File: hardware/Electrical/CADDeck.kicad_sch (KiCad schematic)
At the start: 26 parts, among them SW1L SW_Push, SW1R SW_Push, SW2L SW_Push, SW2R SW_Push, SW3L SW_Push, SW3R SW_Push, SW4L SW_Push, SW4R SW_Push, SW5L SW_Push, SW5R SW_Push, U4 49E Zoom, U5 39E Rotate, U6 TTP223

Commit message: Alles aktualisiert
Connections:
- net at U1. (VDD): now also R6.2, SW3L.2

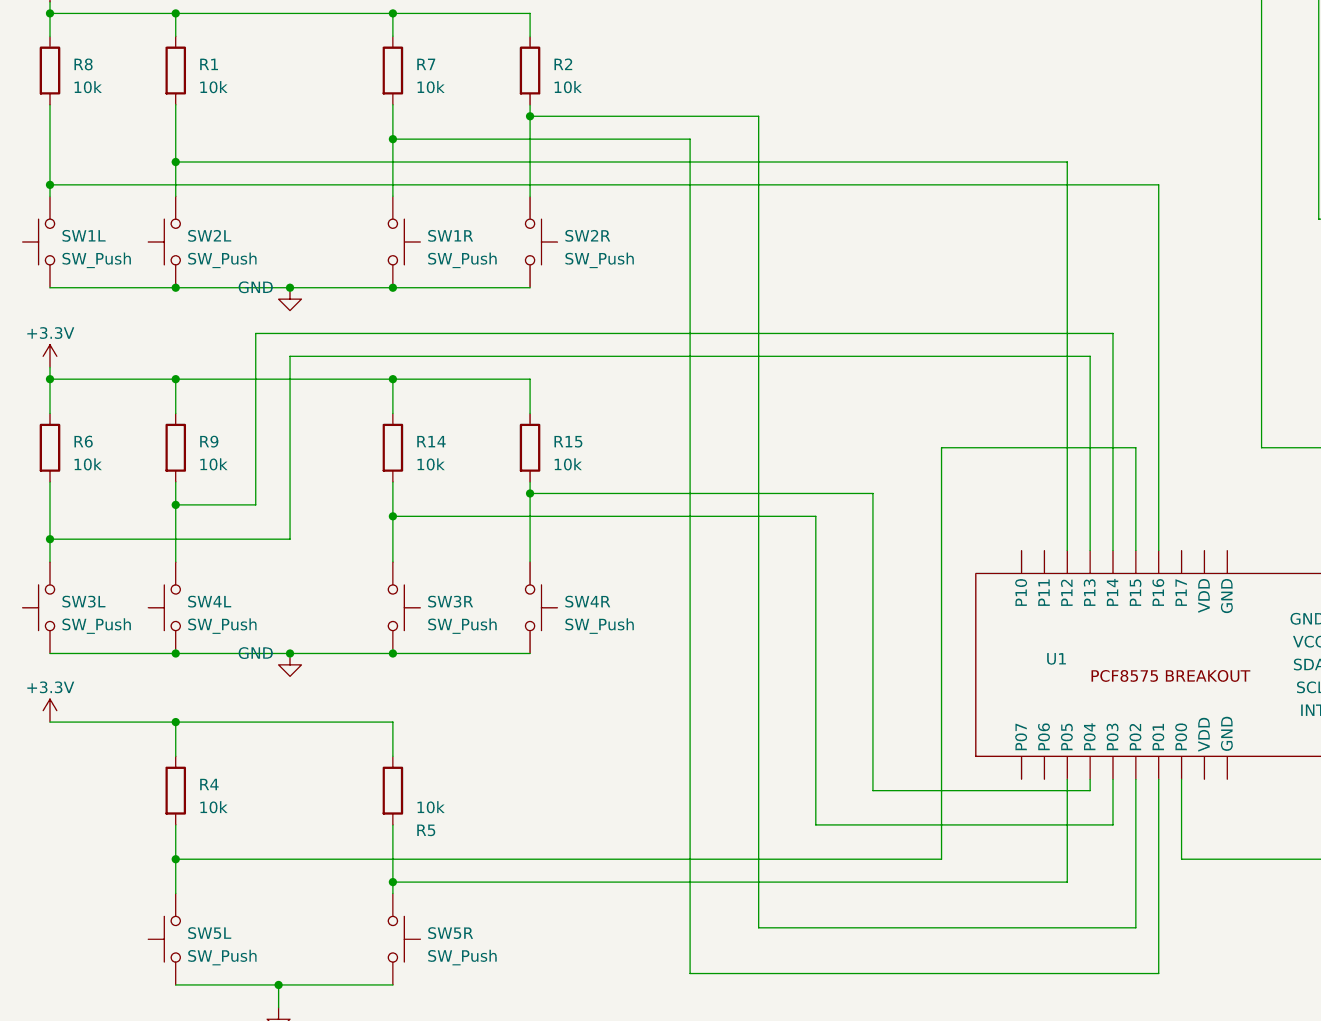
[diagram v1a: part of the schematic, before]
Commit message: Pinbelegung geändert
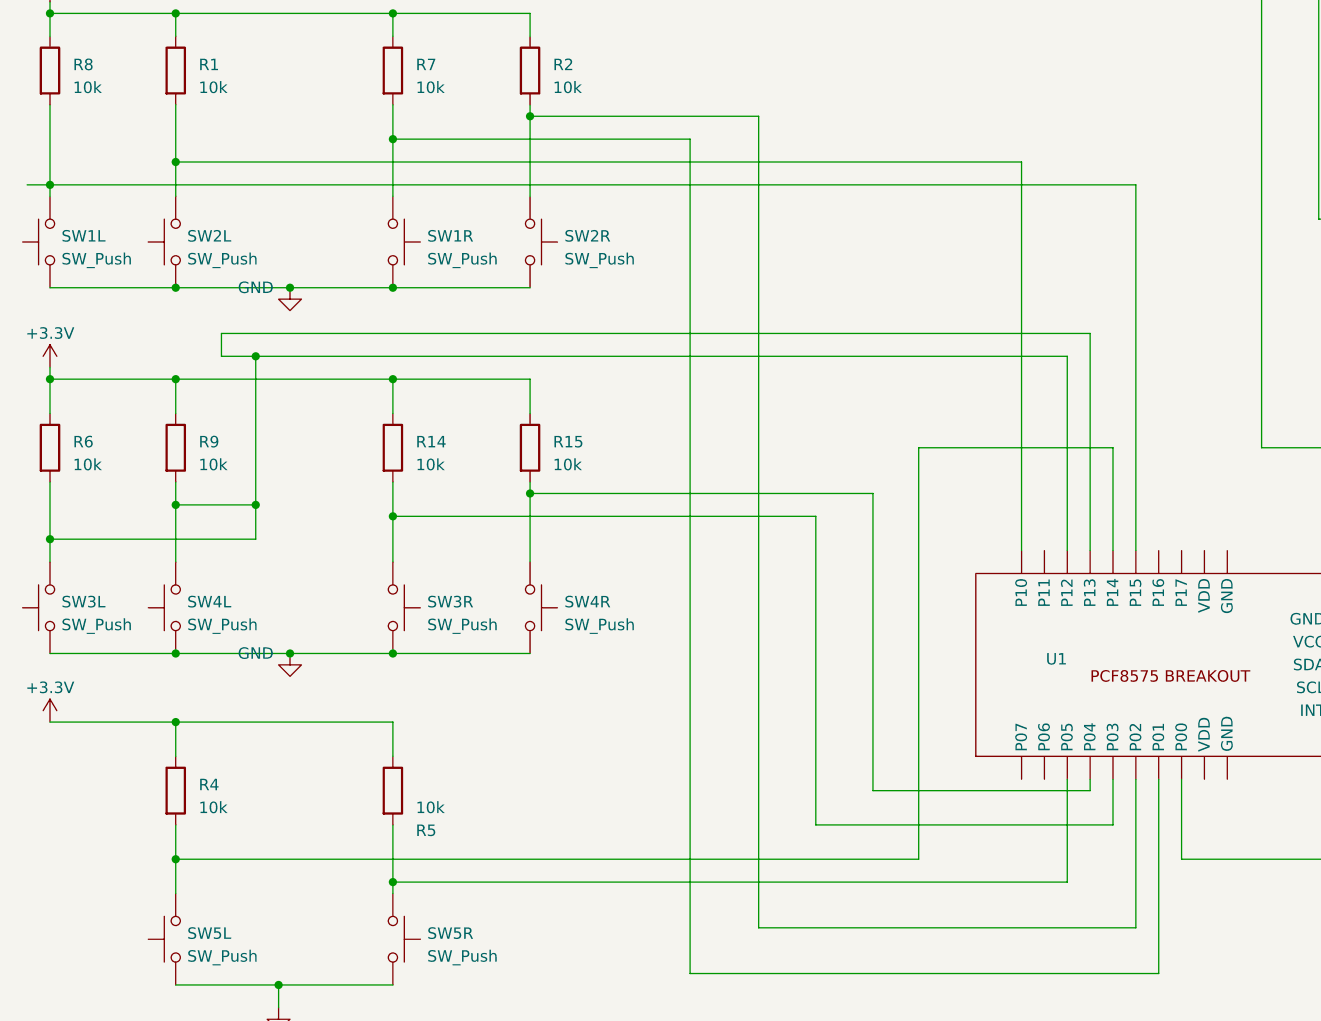
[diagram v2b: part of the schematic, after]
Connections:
- net at U1. (VDD): now also U3.8 (GND)
- net at R9.2, SW4L.2, U1. (VDD): now also R6.2, SW3L.2
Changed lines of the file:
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@@
     (comment 1 "Revised Dirk König")
   )
+  (junction (at 39.37 135.89) (diameter 0) (color 0 0 0 0)
+  )
   (junction (at 16.51 100.33) (diameter 0) (color 0 0 0 0)
   )
@@
   (junction (at 30.48 160.02) (diameter 0) (color 0 0 0 0)
   )
+  (junction (at 39.37 119.38) (diameter 0) (color 0 0 0 0)
+  )
   (junction (at 63.5 33.02) (diameter 0) (color 0 0 0 0)
   )
@@
     (stroke (width 0) (type default))
   )
-  (wire (pts (xy 129.54 140.97) (xy 129.54 97.79))
-    (stroke (width 0) (type default))
-  )
   (wire (pts (xy 30.48 91.44) (xy 30.48 97.79))
     (stroke (width 0) (type default))
@@
     (stroke (width 0) (type default))
   )
+  (wire (pts (xy 39.37 135.89) (xy 39.37 139.7))
+    (stroke (width 0) (type default))
+  )
   (wire (pts (xy 250.19 121.92) (xy 257.81 121.92))
     (stroke (width 0) (type default))
@@
     (stroke (width 0) (type default))
   )
-  (wire (pts (xy 39.37 116.84) (xy 39.37 135.89))
+  (wire (pts (xy 35.56 116.84) (xy 35.56 119.38))
     (stroke (width 0) (type default))
   )
@@
     (stroke (width 0) (type default))
   )
-  (wire (pts (xy 137.16 129.54) (xy 115.57 129.54))
+  (wire (pts (xy 134.62 129.54) (xy 113.03 129.54))
     (stroke (width 0) (type default))
   )
@@
     (stroke (width 0) (type default))
   )
-  (wire (pts (xy 30.48 97.79) (xy 129.54 97.79))
-    (stroke (width 0) (type default))
-  )
-  (wire (pts (xy 43.18 119.38) (xy 43.18 139.7))
+  (wire (pts (xy 30.48 97.79) (xy 124.46 97.79))
     (stroke (width 0) (type default))
   )
@@
     (stroke (width 0) (type default))
   )
-  (wire (pts (xy 134.62 140.97) (xy 134.62 116.84))
-    (stroke (width 0) (type default))
-  )
   (wire (pts (xy 180.34 48.26) (xy 180.34 76.2))
     (stroke (width 0) (type default))
@@
     (stroke (width 0) (type default))
   )
+  (wire (pts (xy 16.51 100.33) (xy 137.16 100.33))
+    (stroke (width 0) (type default))
+  )
   (wire (pts (xy 161.29 151.13) (xy 198.12 151.13))
     (stroke (width 0) (type default))
@@
     (stroke (width 0) (type default))
   )
+  (wire (pts (xy 134.62 129.54) (xy 134.62 140.97))
+    (stroke (width 0) (type default))
+  )
   (wire (pts (xy 52.07 62.23) (xy 52.07 72.39))
     (stroke (width 0) (type default))
@@
     (stroke (width 0) (type default))
   )
+  (wire (pts (xy 35.56 119.38) (xy 39.37 119.38))
+    (stroke (width 0) (type default))
+  )
   (polyline (pts (xy 30.48 15.24) (xy 140.97 15.24))
     (stroke (width 0) (type default))
@@
     (stroke (width 0) (type default))
   )
-  (wire (pts (xy 115.57 129.54) (xy 115.57 175.26))
-    (stroke (width 0) (type default))
-  )
-  (wire (pts (xy 43.18 139.7) (xy 16.51 139.7))
-    (stroke (width 0) (type default))
-  )
-  (wire (pts (xy 132.08 140.97) (xy 132.08 119.38))
+  (wire (pts (xy 113.03 129.54) (xy 113.03 175.26))
+    (stroke (width 0) (type default))
+  )
+  (wire (pts (xy 39.37 139.7) (xy 16.51 139.7))
     (stroke (width 0) (type default))
   )
@@
     (stroke (width 0) (type default))
   )
+  (wire (pts (xy 39.37 119.38) (xy 39.37 135.89))
+    (stroke (width 0) (type default))
+  )
   (wire (pts (xy 16.51 121.92) (xy 16.51 125.73))
     (stroke (width 0) (type default))
@@
     (stroke (width 0) (type default))
   )
-  (wire (pts (xy 132.08 119.38) (xy 43.18 119.38))
+  (wire (pts (xy 39.37 119.38) (xy 129.54 119.38))
     (stroke (width 0) (type default))
   )
@@
     (stroke (width 0) (type default))
   )
-  (wire (pts (xy 16.51 100.33) (xy 139.7 100.33))
-    (stroke (width 0) (type default))
-  )
   (wire (pts (xy 180.34 76.2) (xy 256.54 76.2))
     (stroke (width 0) (type default))
@@
     (stroke (width 0) (type default))
   )
-  (wire (pts (xy 137.16 129.54) (xy 137.16 140.97))
-    (stroke (width 0) (type default))
-  )
   (wire (pts (xy 43.18 152.4) (xy 54.61 152.4))
     (stroke (width 0) (type default))
   )
-  (wire (pts (xy 139.7 100.33) (xy 139.7 140.97))
-    (stroke (width 0) (type default))
-  )
   (wire (pts (xy 64.77 48.26) (xy 64.77 71.12))
     (stroke (width 0) (type default))
@@
     (stroke (width 0) (type default))
   )
-  (wire (pts (xy 134.62 116.84) (xy 39.37 116.84))
+  (wire (pts (xy 132.08 116.84) (xy 132.08 140.97))
+    (stroke (width 0) (type default))
+  )
+  (wire (pts (xy 35.56 116.84) (xy 132.08 116.84))
     (stroke (width 0) (type default))
   )
@@
     (stroke (width 0) (type default))
   )
+  (wire (pts (xy 129.54 119.38) (xy 129.54 140.97))
+    (stroke (width 0) (type default))
+  )
   (wire (pts (xy 151.13 129.54) (xy 167.64 129.54))
     (stroke (width 0) (type default))
@@
     (stroke (width 0) (type default))
   )
-  (wire (pts (xy 115.57 175.26) (xy 30.48 175.26))
+  (wire (pts (xy 113.03 175.26) (xy 30.48 175.26))
     (stroke (width 0) (type default))
   )
@@
     (stroke (width 0) (type default))
   )
+  (wire (pts (xy 137.16 100.33) (xy 137.16 140.97))
+    (stroke (width 0) (type default))
+  )
   (wire (pts (xy 41.91 189.23) (xy 54.61 189.23))
     (stroke (width 0) (type default))
@@
     (stroke (width 0) (type default))
   )
+  (wire (pts (xy 124.46 97.79) (xy 124.46 140.97))
+    (stroke (width 0) (type default))
+  )
   (wire (pts (xy 198.12 139.7) (xy 209.55 139.7))
     (stroke (width 0) (type default))
@@
     (stroke (width 0) (type default))
   )
+  (wire (pts (xy 13.97 100.33) (xy 16.51 100.33))
+    (stroke (width 0) (type default))
+  )

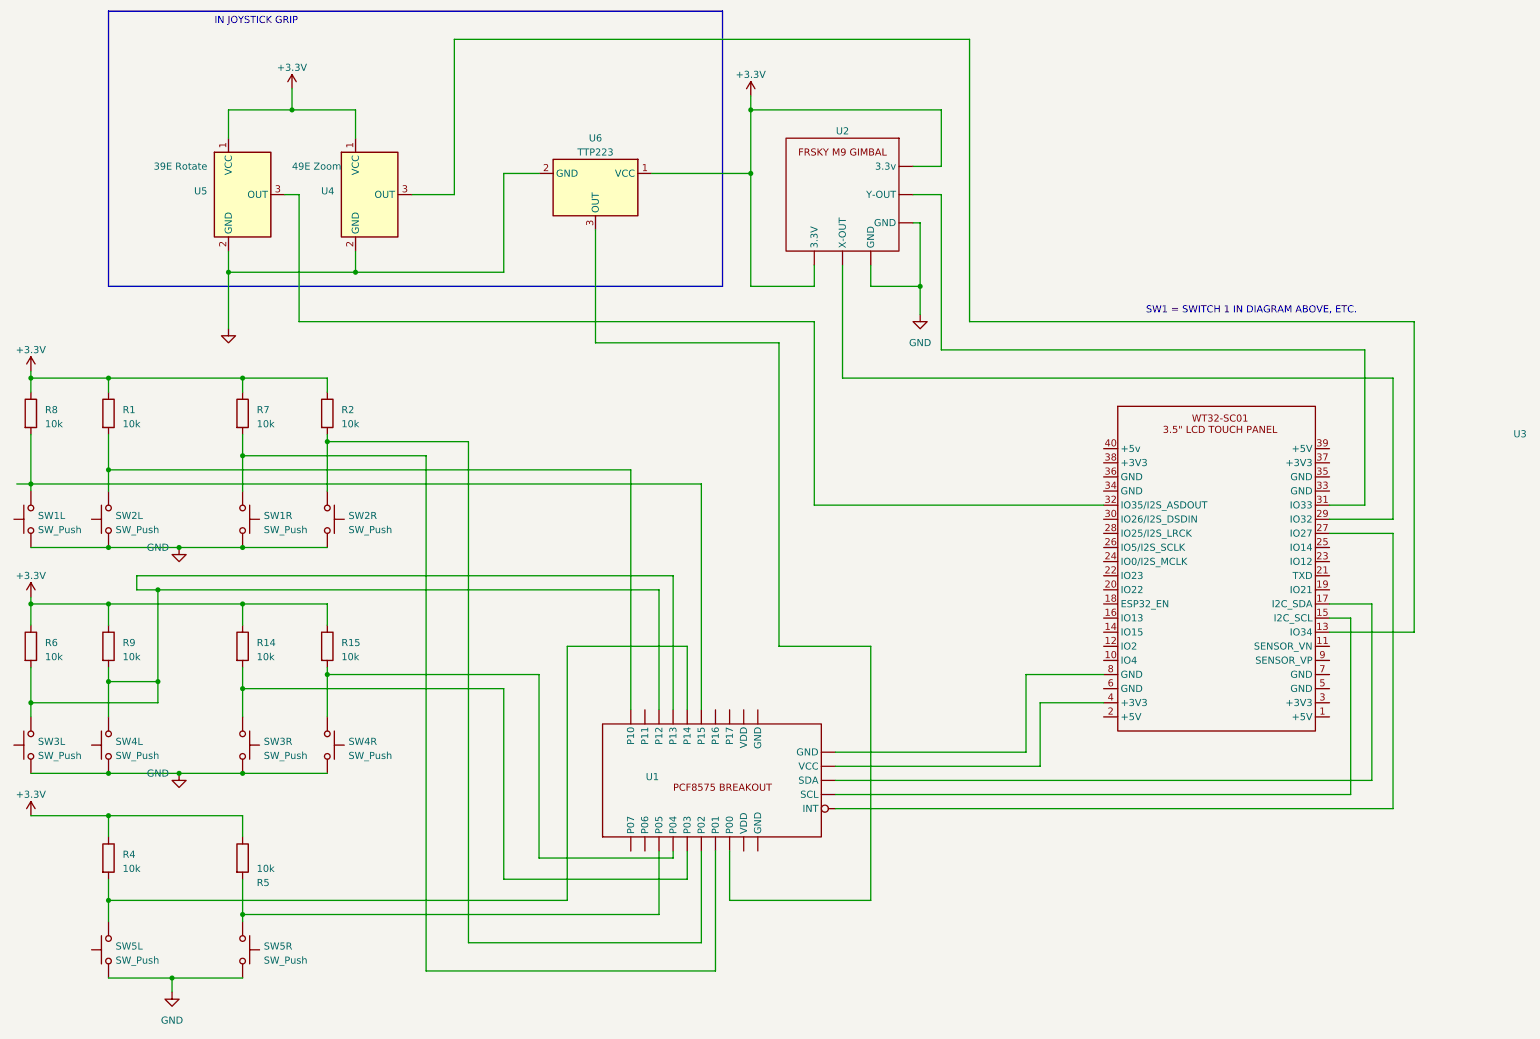
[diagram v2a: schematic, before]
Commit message: Aktuelle Version mit 10 Buttons
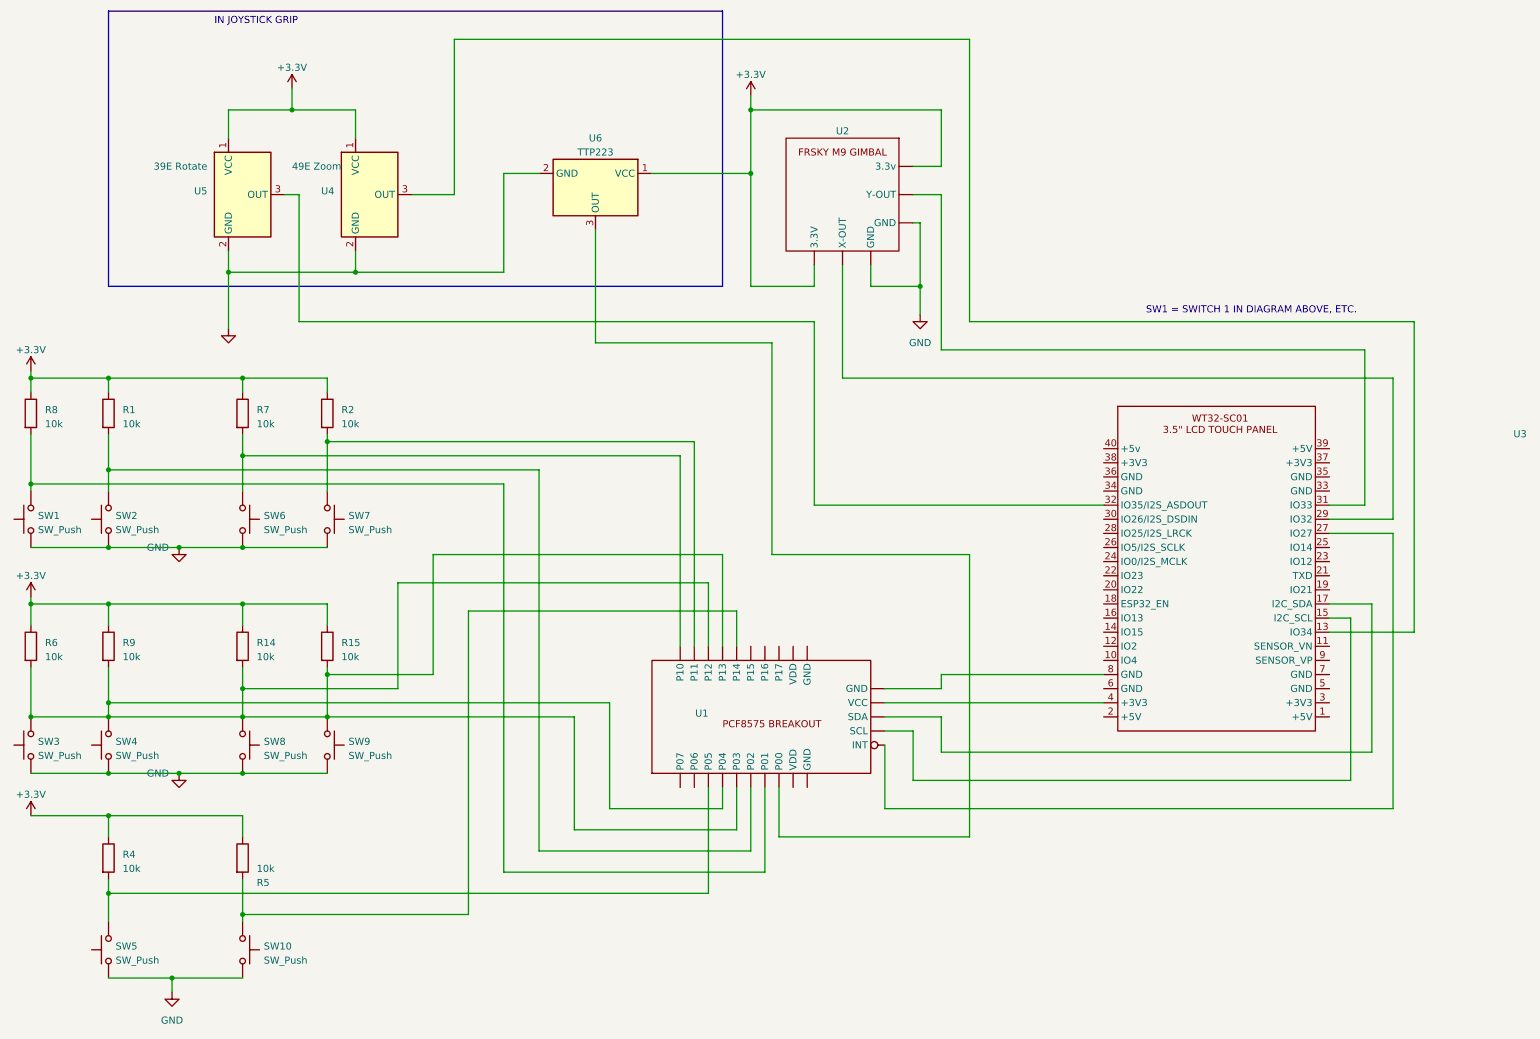
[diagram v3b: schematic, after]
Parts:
- renumbered SW1L to SW1, SW5R to SW10, SW2L to SW2, SW3L to SW3, SW4L to SW4, SW5L to SW5, SW1R to SW6, SW2R to SW7, SW3R to SW8, SW4R to SW9
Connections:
- net at U1. (VDD): now also U3.8 (GND)
- net at R14.2, SW8.1, U1. (VDD): now also R15.2, R6.2, R9.2, SW3.2, SW4.2, SW9.1
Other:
- moved on the sheet: U1

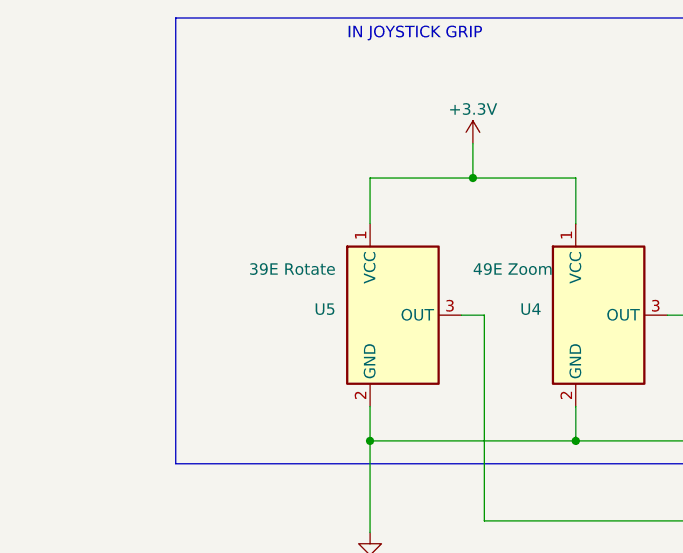
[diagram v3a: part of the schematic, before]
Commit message: Hallsensor hatte die falsche Bezeichnung
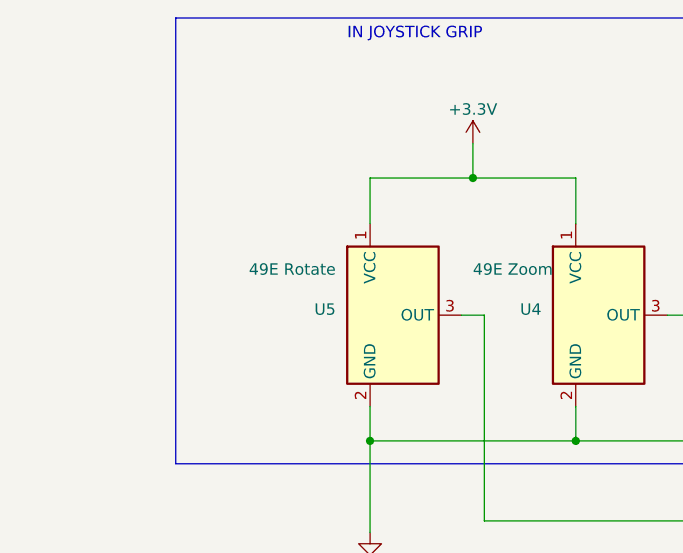
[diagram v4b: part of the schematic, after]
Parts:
- U5: value 39E Rotate -> 49E Rotate
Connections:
- net at U1. (VDD): now also U3.8 (GND)
